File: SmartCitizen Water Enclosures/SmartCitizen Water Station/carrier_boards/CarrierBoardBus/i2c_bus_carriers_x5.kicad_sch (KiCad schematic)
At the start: 6 parts, among them J1 Conn_PinHeader_1x05_P2.54mm_V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, J2 Conn_PinHeader_1x05_P2.54mm_V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, J3 Conn_PinHeader_1x05_P2.54mm_V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, J4 Conn_PinHeader_1x05_P2.54mm_V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, J5 Conn_PinHeader_1x05_P2.54mm_V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, J6 GROVE-CONNECTOR-SMD-90D_4+2P-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

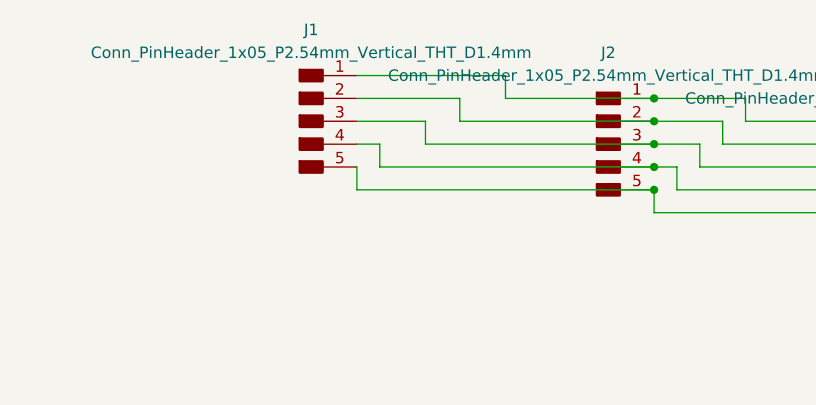
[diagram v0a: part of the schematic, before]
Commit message: Add silkscreen to carrier boards
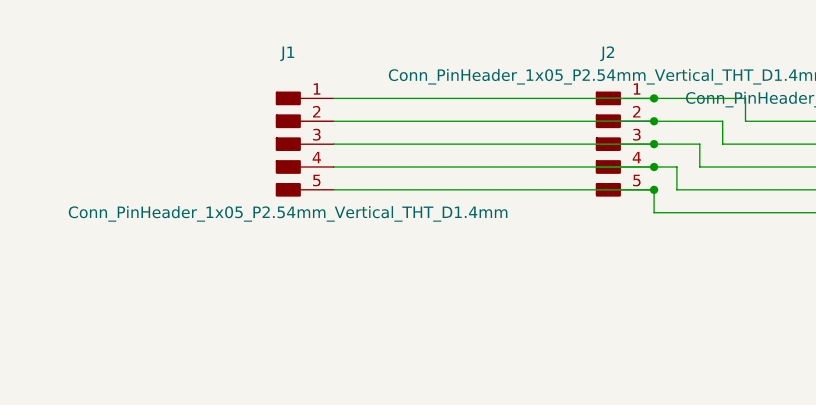
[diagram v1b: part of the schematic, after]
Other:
- moved on the sheet: J1
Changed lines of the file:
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@@
   (junction (at 146.05 48.26) (diameter 0) (color 0 0 0 0)
   )
-  (wire (pts (xy 58.42 40.64) (xy 80.01 40.64))
+  (wire (pts (xy 44.45 40.64) (xy 80.01 40.64))
     (stroke (width 0) (type default))
   )
@@
     (stroke (width 0) (type default))
   )
-  (wire (pts (xy 49.53 45.72) (xy 80.01 45.72))
-    (stroke (width 0) (type default))
-  )
-  (wire (pts (xy 54.61 43.18) (xy 80.01 43.18))
+  (wire (pts (xy 44.45 45.72) (xy 80.01 45.72))
+    (stroke (width 0) (type default))
+  )
+  (wire (pts (xy 44.45 43.18) (xy 80.01 43.18))
     (stroke (width 0) (type default))
   )
@@
     (stroke (width 0) (type default))
   )
-  (wire (pts (xy 46.99 35.56) (xy 63.5 35.56))
-    (stroke (width 0) (type default))
-  )
-  (wire (pts (xy 46.99 45.72) (xy 46.99 48.26))
-    (stroke (width 0) (type default))
-  )
   (wire (pts (xy 80.01 50.8) (xy 113.03 50.8))
     (stroke (width 0) (type default))
   )
-  (wire (pts (xy 49.53 43.18) (xy 49.53 45.72))
-    (stroke (width 0) (type default))
-  )
   (wire (pts (xy 82.55 48.26) (xy 113.03 48.26))
     (stroke (width 0) (type default))
@@
     (stroke (width 0) (type default))
   )
-  (wire (pts (xy 58.42 38.1) (xy 58.42 40.64))
-    (stroke (width 0) (type default))
-  )
   (wire (pts (xy 146.05 55.88) (xy 179.07 55.88))
     (stroke (width 0) (type default))
@@
     (stroke (width 0) (type default))
   )
-  (wire (pts (xy 54.61 40.64) (xy 54.61 43.18))
-    (stroke (width 0) (type default))
-  )
   (wire (pts (xy 146.05 50.8) (xy 151.13 50.8))
     (stroke (width 0) (type default))
@@
     (stroke (width 0) (type default))
   )
-  (wire (pts (xy 46.99 43.18) (xy 49.53 43.18))
-    (stroke (width 0) (type default))
-  )
-  (wire (pts (xy 46.99 48.26) (xy 80.01 48.26))
+  (wire (pts (xy 44.45 48.26) (xy 80.01 48.26))
     (stroke (width 0) (type default))
   )
@@
     (stroke (width 0) (type default))
   )
-  (wire (pts (xy 63.5 38.1) (xy 80.01 38.1))
+  (wire (pts (xy 44.45 38.1) (xy 80.01 38.1))
     (stroke (width 0) (type default))
   )
@@
     (stroke (width 0) (type default))
   )
-  (wire (pts (xy 63.5 35.56) (xy 63.5 38.1))
-    (stroke (width 0) (type default))
-  )
   (wire (pts (xy 113.03 48.26) (xy 113.03 49.53))
     (stroke (width 0) (type default))
@@
   )
   (wire (pts (xy 146.05 49.53) (xy 146.05 50.8))
-    (stroke (width 0) (type default))
-  )
-  (wire (pts (xy 46.99 40.64) (xy 54.61 40.64))
-    (stroke (width 0) (type default))
-  )
-  (wire (pts (xy 46.99 38.1) (xy 58.42 38.1))
     (stroke (width 0) (type default))
   )
@@
     )
   )
-  (symbol (lib_id "fab:Conn_PinHeader_1x05_P2.54mm_Vertical_THT_D1.4mm") (at 41.91 40.64 0) (unit 1)
-    (in_bom yes) (on_board yes) (dnp no) (fields_autoplaced)
-    (property "Reference" "J1" (at 41.91 30.48 0)
-      (effects (font (size 1.27 1.27)))
-    )
-    (property "Value" "Conn_PinHeader_1x05_P2.54mm_Vertical_THT_D1.4mm" (at 41.91 33.02 0)
-      (effects (font (size 1.27 1.27)))
-    )
-    (property "Footprint" "fab:PinHeader_1x05_P2.54mm_Vertical_THT_D1.4mm" (at 41.91 40.64 0)
-      (effects (font (size 1.27 1.27)) hide)
-    )
-    (property "Datasheet" "~" (at 41.91 40.64 0)
-      (effects (font (size 1.27 1.27)) hide)
-    )
+  (symbol (lib_id "fab:Conn_PinHeader_1x05_P2.54mm_Vertical_THT_D1.4mm") (at 39.37 43.18 0) (unit 1)
+    (in_bom yes) (on_board yes) (dnp no)
+    (property "Reference" "J1" (at 39.37 33.02 0)
+      (effects (font (size 1.27 1.27)))
+    )
+    (property "Value" "Conn_PinHeader_1x05_P2.54mm_Vertical_THT_D1.4mm" (at 39.37 50.8 0)
+      (effects (font (size 1.27 1.27)))
+    )
+    (property "Footprint" "fab:PinHeader_1x05_P2.54mm_Vertical_THT_D1.4mm" (at 39.37 43.18 0)
+      (effects (font (size 1.27 1.27)) hide)
+    )
+    (property "Datasheet" "~" (at 39.37 43.18 0)
+      (effects (font (size 1.27 1.27)) hide)
+    )
